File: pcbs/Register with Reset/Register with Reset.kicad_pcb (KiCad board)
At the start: 2 copper layers, 55 parts, among them J101 Conn_02x20_Odd_Even, U201 74HC245, U202 74HCT574, U203 74HC245, U301 74HC245, U302 74HCT574, U303 74HC245

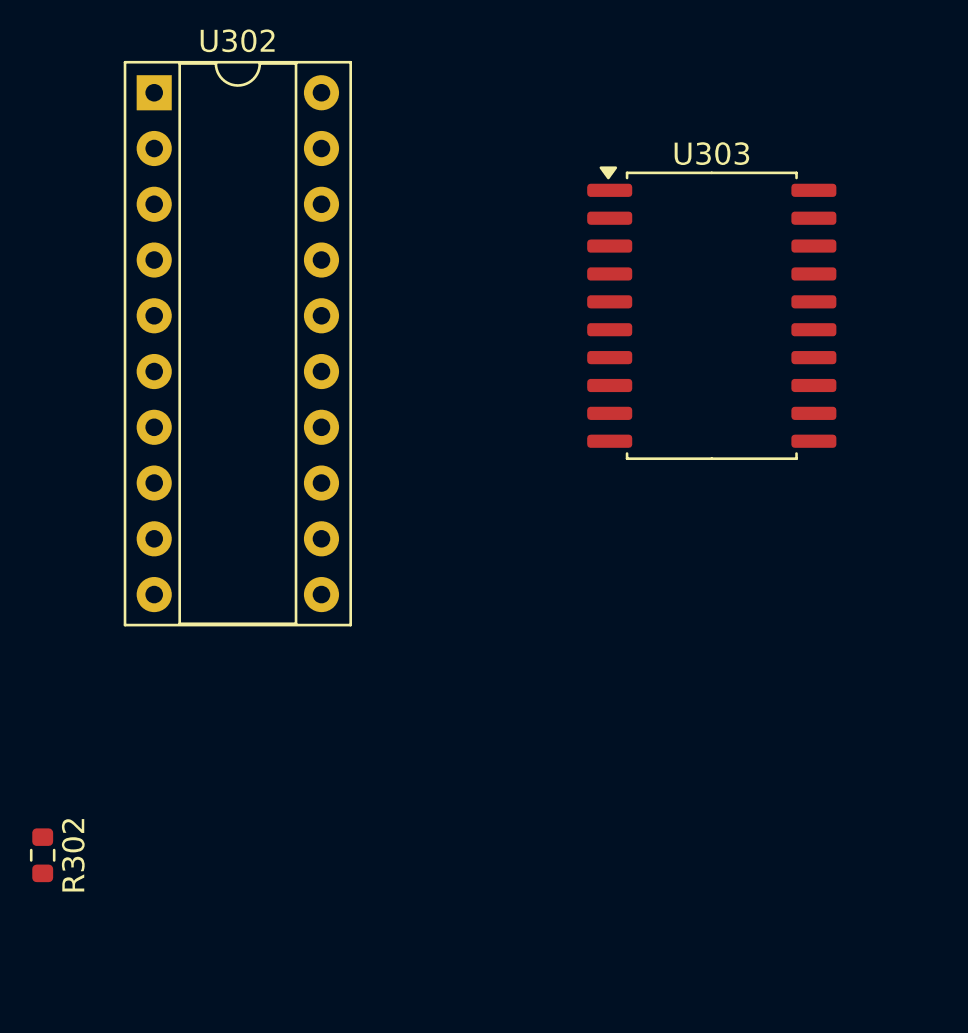
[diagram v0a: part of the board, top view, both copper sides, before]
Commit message: Adding design rules
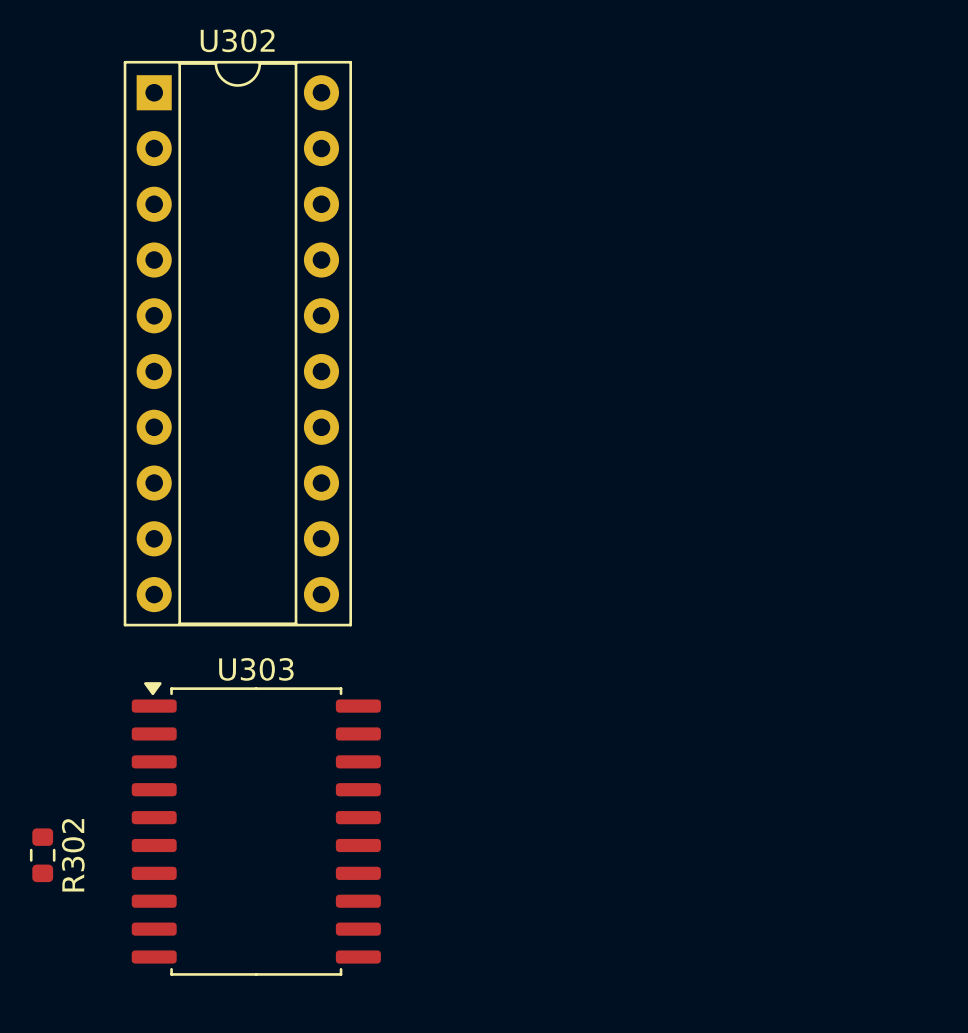
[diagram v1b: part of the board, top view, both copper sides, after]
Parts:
- moved U303 31.3 mm to (131.7, 160.7)
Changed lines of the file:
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@@
 	)
 	(setup
+		(stackup
+			(layer "F.SilkS"
+				(type "Top Silk Screen")
+			)
+			(layer "F.Paste"
+				(type "Top Solder Paste")
+			)
+			(layer "F.Mask"
+				(type "Top Solder Mask")
+				(thickness 0.01)
+			)
+			(layer "F.Cu"
+				(type "copper")
+				(thickness 0.035)
+			)
+			(layer "dielectric 1"
+				(type "core")
+				(thickness 1.51)
+				(material "FR4")
+				(epsilon_r 4.5)
+				(loss_tangent 0.02)
+			)
+			(layer "B.Cu"
+				(type "copper")
+				(thickness 0.035)
+			)
+			(layer "B.Mask"
+				(type "Bottom Solder Mask")
+				(thickness 0.01)
+			)
+			(layer "B.Paste"
+				(type "Bottom Solder Paste")
+			)
+			(layer "B.SilkS"
+				(type "Bottom Silk Screen")
+			)
+			(copper_finish "None")
+			(dielectric_constraints no)
+		)
 		(pad_to_mask_clearance 0)
 		(allow_soldermask_bridges_in_footprints no)
@@
 	(footprint "Package_SO:SOIC-20W_7.5x12.8mm_P1.27mm"
 		(layer "F.Cu")
-		(at 152.4 137.16)
+		(at 131.65 160.655)
 		(descr "SOIC, 20 Pin (JEDEC MS-013AC, https://www.analog.com/media/en/package-pcb-resources/package/233848rw_20.pdf), generated with kicad-footprint-generator ipc_gullwing_generator.py")
 		(tags "SOIC SO")
@@
 		(tags "SOIC SO")
 		(property "Reference" "U201"
-			(at 0 -7.35 360)
+			(at 0 -7.35 0)
 			(layer "F.SilkS")
 			(effects
@@
 		)
 		(property "Value" "74HC245"
-			(at 0 7.35 360)
+			(at 0 7.35 0)
 			(layer "F.Fab")
 			(effects
@@
 		)
 		(fp_text user "${REFERENCE}"
-			(at 0 0 360)
+			(at 0 0 0)
 			(layer "F.Fab")
 			(effects

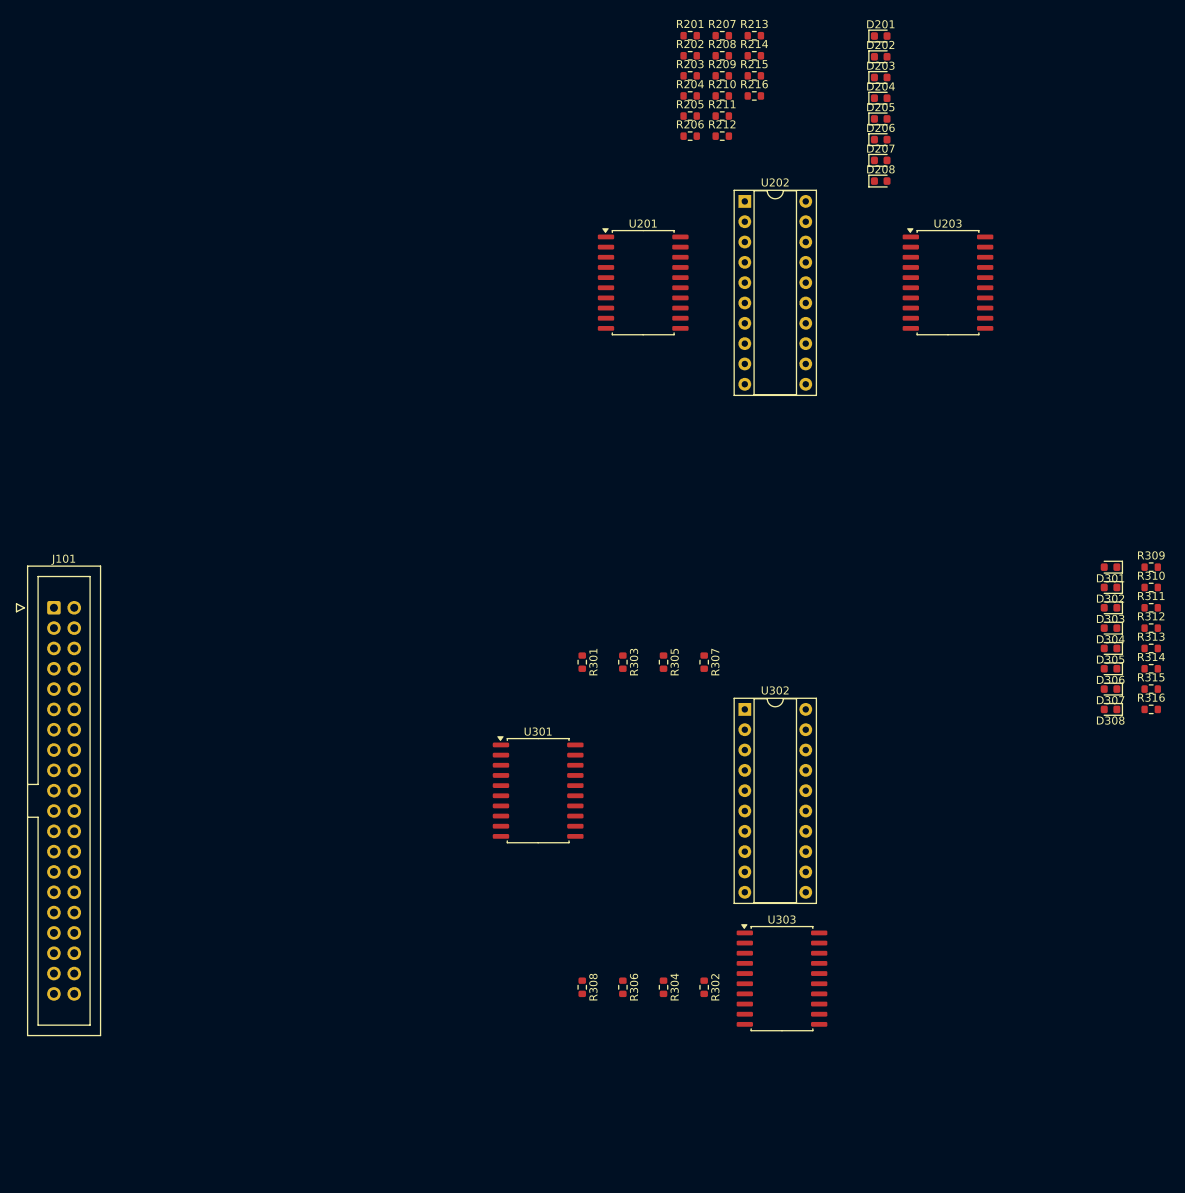
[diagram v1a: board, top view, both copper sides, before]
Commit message: Routing the actual registers
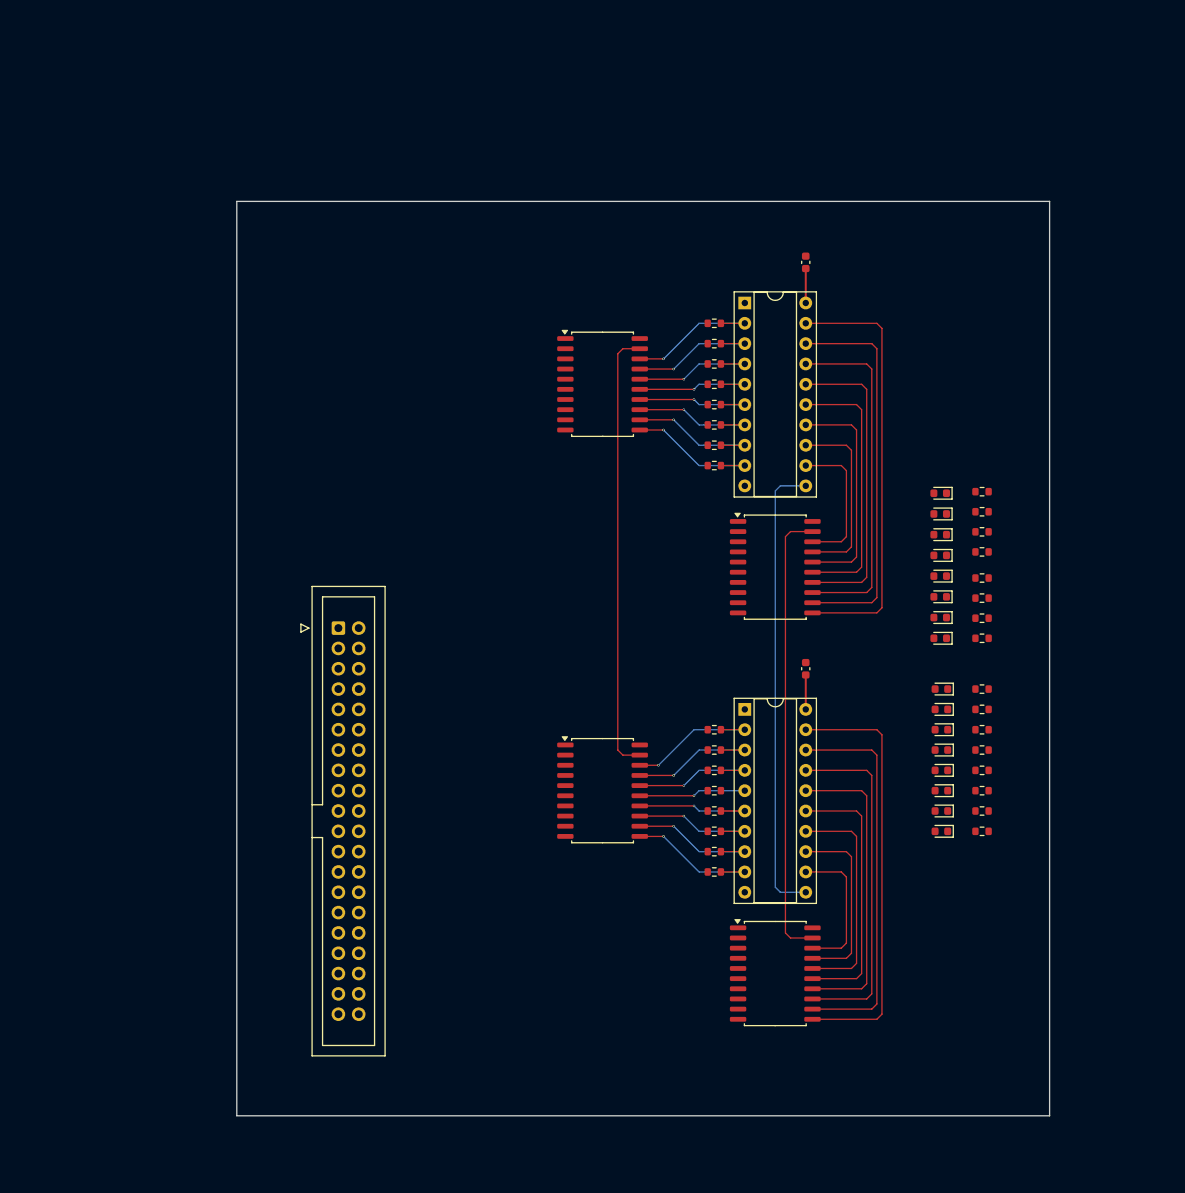
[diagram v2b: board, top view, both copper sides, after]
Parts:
- added C201: C, Capacitor_SMD:C_0603_1608Metric, F.Cu at (134.6, 121.9)
- added C301: C, Capacitor_SMD:C_0603_1608Metric, F.Cu at (134.6, 71.1)
- moved R214 73.5 mm to (156.7, 113.1)
- moved R213 73.5 mm to (156.7, 110.6)
- moved R215 73.5 mm to (156.7, 115.6)
- moved R216 73.5 mm to (156.7, 118.1)
- moved R211 61.3 mm to (156.7, 104.8)
- moved R210 61.3 mm to (156.7, 102.3)
- moved R209 61.3 mm to (156.7, 99.8)
- moved R212 61.3 mm to (156.7, 107.3)
- moved D201 57.6 mm to (151.4, 100.0), turned to 180 degrees
- moved D205 57.6 mm to (151.4, 110.3), turned to 180 degrees
- moved D206 57.6 mm to (151.4, 112.9), turned to 180 degrees
- moved D203 57.6 mm to (151.4, 105.2), turned to 180 degrees
- moved D204 57.6 mm to (151.4, 107.8), turned to 180 degrees
- moved D207 57.6 mm to (151.4, 115.5), turned to 180 degrees
- moved D208 57.6 mm to (151.4, 118.1), turned to 180 degrees
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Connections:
- R202 pad 1: Net-(U201-B4) -> Net-(U201-B1)
- R203 pad 2: Net-(U201-B1) -> Net-(U201-B2)
- R204 pad 1: Net-(U201-B5) -> Net-(U201-B3)
- R205 pad 2: Net-(U201-B2) -> Net-(U201-B4)
- R206 pad 1: Net-(U201-B6) -> Net-(U201-B5)
- R207 pad 2: Net-(U201-B3) -> Net-(U201-B6)
- R302 pad 1: Net-(U301-B4) -> Net-(U301-B1)
- R303 pad 2: Net-(U301-B1) -> Net-(U301-B2)
- R304 pad 1: Net-(U301-B5) -> Net-(U301-B3)
- R305 pad 2: Net-(U301-B2) -> Net-(U301-B4)
- R306 pad 1: Net-(U301-B6) -> Net-(U301-B5)
- R307 pad 2: Net-(U301-B3) -> Net-(U301-B6)
- U201 pad 19: unconnected-(U201-CE-Pad19) -> /Register 0/~{ZeroInput}
- U202 pad 11: unconnected-(U202-Cp-Pad11) -> /Register 0/RegClk
- U203 pad 1: +5V -> GND
- U203 pad 11: /Register 0/Out7 -> Net-(D201-A)
- U203 pad 12: /Register 0/Out6 -> Net-(D202-A)
- U203 pad 13: /Register 0/Out5 -> Net-(D203-A)
- U203 pad 14: /Register 0/Out4 -> Net-(D204-A)
- U203 pad 15: /Register 0/Out3 -> Net-(D205-A)
- U203 pad 16: /Register 0/Out2 -> Net-(D206-A)
- U203 pad 17: /Register 0/Out1 -> Net-(D207-A)
- U203 pad 18: /Register 0/Out0 -> Net-(D208-A)
- U203 pad 19: unconnected-(U203-CE-Pad19) -> /Register 0/~{OE}
- U203 pad 2: Net-(D201-A) -> /Register 0/Out7
- U203 pad 3: Net-(D202-A) -> /Register 0/Out6
- U203 pad 4: Net-(D203-A) -> /Register 0/Out5
- U203 pad 5: Net-(D204-A) -> /Register 0/Out4
- U203 pad 6: Net-(D205-A) -> /Register 0/Out3
- U203 pad 7: Net-(D206-A) -> /Register 0/Out2
- U203 pad 8: Net-(D207-A) -> /Register 0/Out1
- U203 pad 9: Net-(D208-A) -> /Register 0/Out0
- U301 pad 19: unconnected-(U301-CE-Pad19) -> /Register 0/~{ZeroInput}
- U302 pad 11: unconnected-(U302-Cp-Pad11) -> /Register 0/RegClk
- U303 pad 1: +5V -> GND
- U303 pad 11: /Register 1/Out7 -> Net-(D301-A)
- U303 pad 12: /Register 1/Out6 -> Net-(D302-A)
- U303 pad 13: /Register 1/Out5 -> Net-(D303-A)
- U303 pad 14: /Register 1/Out4 -> Net-(D304-A)
- U303 pad 15: /Register 1/Out3 -> Net-(D305-A)
- U303 pad 16: /Register 1/Out2 -> Net-(D306-A)
- U303 pad 17: /Register 1/Out1 -> Net-(D307-A)
- U303 pad 18: /Register 1/Out0 -> Net-(D308-A)
- U303 pad 19: unconnected-(U303-CE-Pad19) -> /Register 0/~{OE}
- U303 pad 2: Net-(D301-A) -> /Register 1/Out7
- U303 pad 3: Net-(D302-A) -> /Register 1/Out6
- U303 pad 4: Net-(D303-A) -> /Register 1/Out5
- U303 pad 5: Net-(D304-A) -> /Register 1/Out4
- U303 pad 6: Net-(D305-A) -> /Register 1/Out3
- U303 pad 7: Net-(D306-A) -> /Register 1/Out2
- U303 pad 8: Net-(D307-A) -> /Register 1/Out1
- U303 pad 9: Net-(D308-A) -> /Register 1/Out0
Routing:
- net /Register 0/RegClk: track 0.00 -> 57.7 mm
- net /Register 0/~{OE}: track 0.00 -> 56.8 mm
- net /Register 0/~{ZeroInput}: track 0.00 -> 55.5 mm
- net Net-(D301-A): track 0.00 -> 53.7 mm
- net Net-(D201-A): track 0.00 -> 53.7 mm
- net Net-(D302-A): track 0.00 -> 48.6 mm
- net Net-(D202-A): track 0.00 -> 48.6 mm
- net Net-(D303-A): track 0.00 -> 43.5 mm
- net Net-(D203-A): track 0.00 -> 43.5 mm
- net Net-(D304-A): track 0.00 -> 38.4 mm
- net Net-(D204-A): track 0.00 -> 38.4 mm
- net Net-(D305-A): track 0.00 -> 33.3 mm
- net Net-(D205-A): track 0.00 -> 33.3 mm
- net Net-(D206-A): track 0.00 -> 28.3 mm
- net Net-(D306-A): track 0.00 -> 28.3 mm
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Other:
- board outline added: 101.6 x 114.3 mm

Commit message: Working on reset logic and some routing
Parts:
- added C401: 10u, Capacitor_SMD:C_0603_1608Metric, F.Cu at (73.0, 79.2)
- added C402: 1u, Capacitor_SMD:C_0603_1608Metric, F.Cu at (88.3, 90.6)
- added C403: 1u, Capacitor_SMD:C_0603_1608Metric, F.Cu at (88.3, 94.4)
- added H101: MountingHole, MountingHole:MountingHole_2.7mm_M2.5, F.Cu at (67.3, 67.3)
- added H102: MountingHole, MountingHole:MountingHole_2.7mm_M2.5, F.Cu at (161.3, 67.3)
- added H103: MountingHole, MountingHole:MountingHole_2.7mm_M2.5, F.Cu at (67.3, 174.0)
- added H104: MountingHole, MountingHole:MountingHole_2.7mm_M2.5, F.Cu at (161.3, 174.0)
- added R401: 11k, Resistor_SMD:R_0603_1608Metric, F.Cu at (73.0, 81.7)
- added R402: 1M, Resistor_SMD:R_0603_1608Metric, F.Cu at (73.0, 84.3)
- added R403: 1M, Resistor_SMD:R_0603_1608Metric, F.Cu at (73.0, 76.6)
- added R404: 11k, Resistor_SMD:R_0603_1608Metric, F.Cu at (85.7, 90.6)
- added R405: 1M, Resistor_SMD:R_0603_1608Metric, F.Cu at (90.8, 90.6)
- added R406: 11k, Resistor_SMD:R_0603_1608Metric, F.Cu at (85.7, 94.4)
- added R407: 1M, Resistor_SMD:R_0603_1608Metric, F.Cu at (90.8, 94.4)
- added U401: 74HC08, Package_SO:SOIC-14_3.9x8.7mm_P1.27mm, F.Cu at (79.4, 80.0)
- added U402: 74HC14, Package_SO:SOIC-14_3.9x8.7mm_P1.27mm, F.Cu at (79.4, 92.7)
- moved J101 13.5 mm to (67.3, 106.7)
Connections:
- J101 pad 10: unconnected-(J101-Pin_10-Pad10) -> /Reg0.In7
- J101 pad 11: unconnected-(J101-Pin_11-Pad11) -> /Reg1.In0
- J101 pad 12: unconnected-(J101-Pin_12-Pad12) -> /Reg1.In1
- J101 pad 13: unconnected-(J101-Pin_13-Pad13) -> /Reg1.In2
- J101 pad 14: unconnected-(J101-Pin_14-Pad14) -> /Reg1.In3
- J101 pad 15: unconnected-(J101-Pin_15-Pad15) -> /Reg1.In4
- J101 pad 16: unconnected-(J101-Pin_16-Pad16) -> /Reg1.In5
- J101 pad 17: unconnected-(J101-Pin_17-Pad17) -> /Reg1.In6
- J101 pad 18: unconnected-(J101-Pin_18-Pad18) -> /Reg1.In7
- J101 pad 23: unconnected-(J101-Pin_23-Pad23) -> /Reg0.Out0
- J101 pad 24: unconnected-(J101-Pin_24-Pad24) -> /Reg0.Out1
- J101 pad 25: unconnected-(J101-Pin_25-Pad25) -> /Reg0.Out2
- J101 pad 26: unconnected-(J101-Pin_26-Pad26) -> /Reg0.Out3
- J101 pad 27: unconnected-(J101-Pin_27-Pad27) -> /Reg0.Out4
- J101 pad 28: unconnected-(J101-Pin_28-Pad28) -> /Reg0.Out5
- J101 pad 29: unconnected-(J101-Pin_29-Pad29) -> /Reg0.Out6
- J101 pad 3: unconnected-(J101-Pin_3-Pad3) -> /Reg0.In0
- J101 pad 30: unconnected-(J101-Pin_30-Pad30) -> /Reg0.Out7
- J101 pad 31: unconnected-(J101-Pin_31-Pad31) -> /Reg1.Out0
- J101 pad 32: unconnected-(J101-Pin_32-Pad32) -> /Reg1.Out1
- J101 pad 33: unconnected-(J101-Pin_33-Pad33) -> /Reg1.Out2
- J101 pad 34: unconnected-(J101-Pin_34-Pad34) -> /Reg1.Out3
- J101 pad 35: unconnected-(J101-Pin_35-Pad35) -> /Reg1.Out4
- J101 pad 36: unconnected-(J101-Pin_36-Pad36) -> /Reg1.Out5
- J101 pad 37: unconnected-(J101-Pin_37-Pad37) -> /Reg1.Out6
- J101 pad 38: unconnected-(J101-Pin_38-Pad38) -> /Reg1.Out7
- J101 pad 4: unconnected-(J101-Pin_4-Pad4) -> /Reg0.In1
- J101 pad 5: unconnected-(J101-Pin_5-Pad5) -> /Reg0.In2
- J101 pad 6: unconnected-(J101-Pin_6-Pad6) -> /Reg0.In3
- J101 pad 7: unconnected-(J101-Pin_7-Pad7) -> /Reg0.In4
- J101 pad 8: unconnected-(J101-Pin_8-Pad8) -> /Reg0.In5
- J101 pad 9: unconnected-(J101-Pin_9-Pad9) -> /Reg0.In6
- U201 pad 2: /Register 0/In0 -> /Reg0.In0
- U201 pad 3: /Register 0/In1 -> /Reg0.In1
- U201 pad 4: /Register 0/In2 -> /Reg0.In2
- U201 pad 5: /Register 0/In3 -> /Reg0.In3
- U201 pad 6: /Register 0/In4 -> /Reg0.In4
- U201 pad 7: /Register 0/In5 -> /Reg0.In5
- U201 pad 8: /Register 0/In6 -> /Reg0.In6
- U201 pad 9: /Register 0/In7 -> /Reg0.In7
- U203 pad 2: /Register 0/Out7 -> /Reg0.Out7
- U203 pad 3: /Register 0/Out6 -> /Reg0.Out6
- U203 pad 4: /Register 0/Out5 -> /Reg0.Out5
- U203 pad 5: /Register 0/Out4 -> /Reg0.Out4
- U203 pad 6: /Register 0/Out3 -> /Reg0.Out3
- U203 pad 7: /Register 0/Out2 -> /Reg0.Out2
- U203 pad 8: /Register 0/Out1 -> /Reg0.Out1
- U203 pad 9: /Register 0/Out0 -> /Reg0.Out0
- U301 pad 2: /Register 1/In0 -> /Reg1.In0
- U301 pad 3: /Register 1/In1 -> /Reg1.In1
- U301 pad 4: /Register 1/In2 -> /Reg1.In2
- U301 pad 5: /Register 1/In3 -> /Reg1.In3
- U301 pad 6: /Register 1/In4 -> /Reg1.In4
- U301 pad 7: /Register 1/In5 -> /Reg1.In5
- U301 pad 8: /Register 1/In6 -> /Reg1.In6
- U301 pad 9: /Register 1/In7 -> /Reg1.In7
- U303 pad 2: /Register 1/Out7 -> /Reg1.Out7
- U303 pad 3: /Register 1/Out6 -> /Reg1.Out6
- U303 pad 4: /Register 1/Out5 -> /Reg1.Out5
- U303 pad 5: /Register 1/Out4 -> /Reg1.Out4
- U303 pad 6: /Register 1/Out3 -> /Reg1.Out3
- U303 pad 7: /Register 1/Out2 -> /Reg1.Out2
- U303 pad 8: /Register 1/Out1 -> /Reg1.Out1
- U303 pad 9: /Register 1/Out0 -> /Reg1.Out0
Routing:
- net /Reg0.Out7: track 0.00 -> 68.4 mm, vias 0 -> 1
- net /Reg0.Out6: track 0.00 -> 65.2 mm, vias 0 -> 1
- net /Reg0.Out5: track 0.00 -> 62.0 mm, vias 0 -> 1
- net /Reg0.Out4: track 0.00 -> 58.9 mm, vias 0 -> 1
- net /Reg0.Out3: track 0.00 -> 55.7 mm, vias 0 -> 1
- net /Reg0.Out2: track 0.00 -> 52.5 mm, vias 0 -> 1
- net /Reg0.Out1: track 0.00 -> 50.0 mm, vias 0 -> 1
- net /Reg0.Out0: track 0.00 -> 46.8 mm, vias 0 -> 1
- net /Reg0.In0: track 0.00 -> 27.1 mm, vias 0 -> 1
- net /Reg0.In1: track 0.00 -> 25.2 mm, vias 0 -> 1
- net /Reg0.In2: track 0.00 -> 23.3 mm, vias 0 -> 1
- net /Reg1.In7: track 0.00 -> 22.0 mm, vias 0 -> 1
- net /Reg0.In3: track 0.00 -> 21.4 mm, vias 0 -> 1
- net /Reg1.In6: track 0.00 -> 20.1 mm, vias 0 -> 1
- net /Reg0.In4: track 0.00 -> 19.5 mm, vias 0 -> 1
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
